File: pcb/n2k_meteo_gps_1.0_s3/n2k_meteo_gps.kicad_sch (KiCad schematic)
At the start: 33 parts, among them J10 3.3-5V, U1 LM7805_TO220, U2 ESP32-S3_SUPERMINI, U3 MCP2562-E-P, U4 PC817, U6 PC817

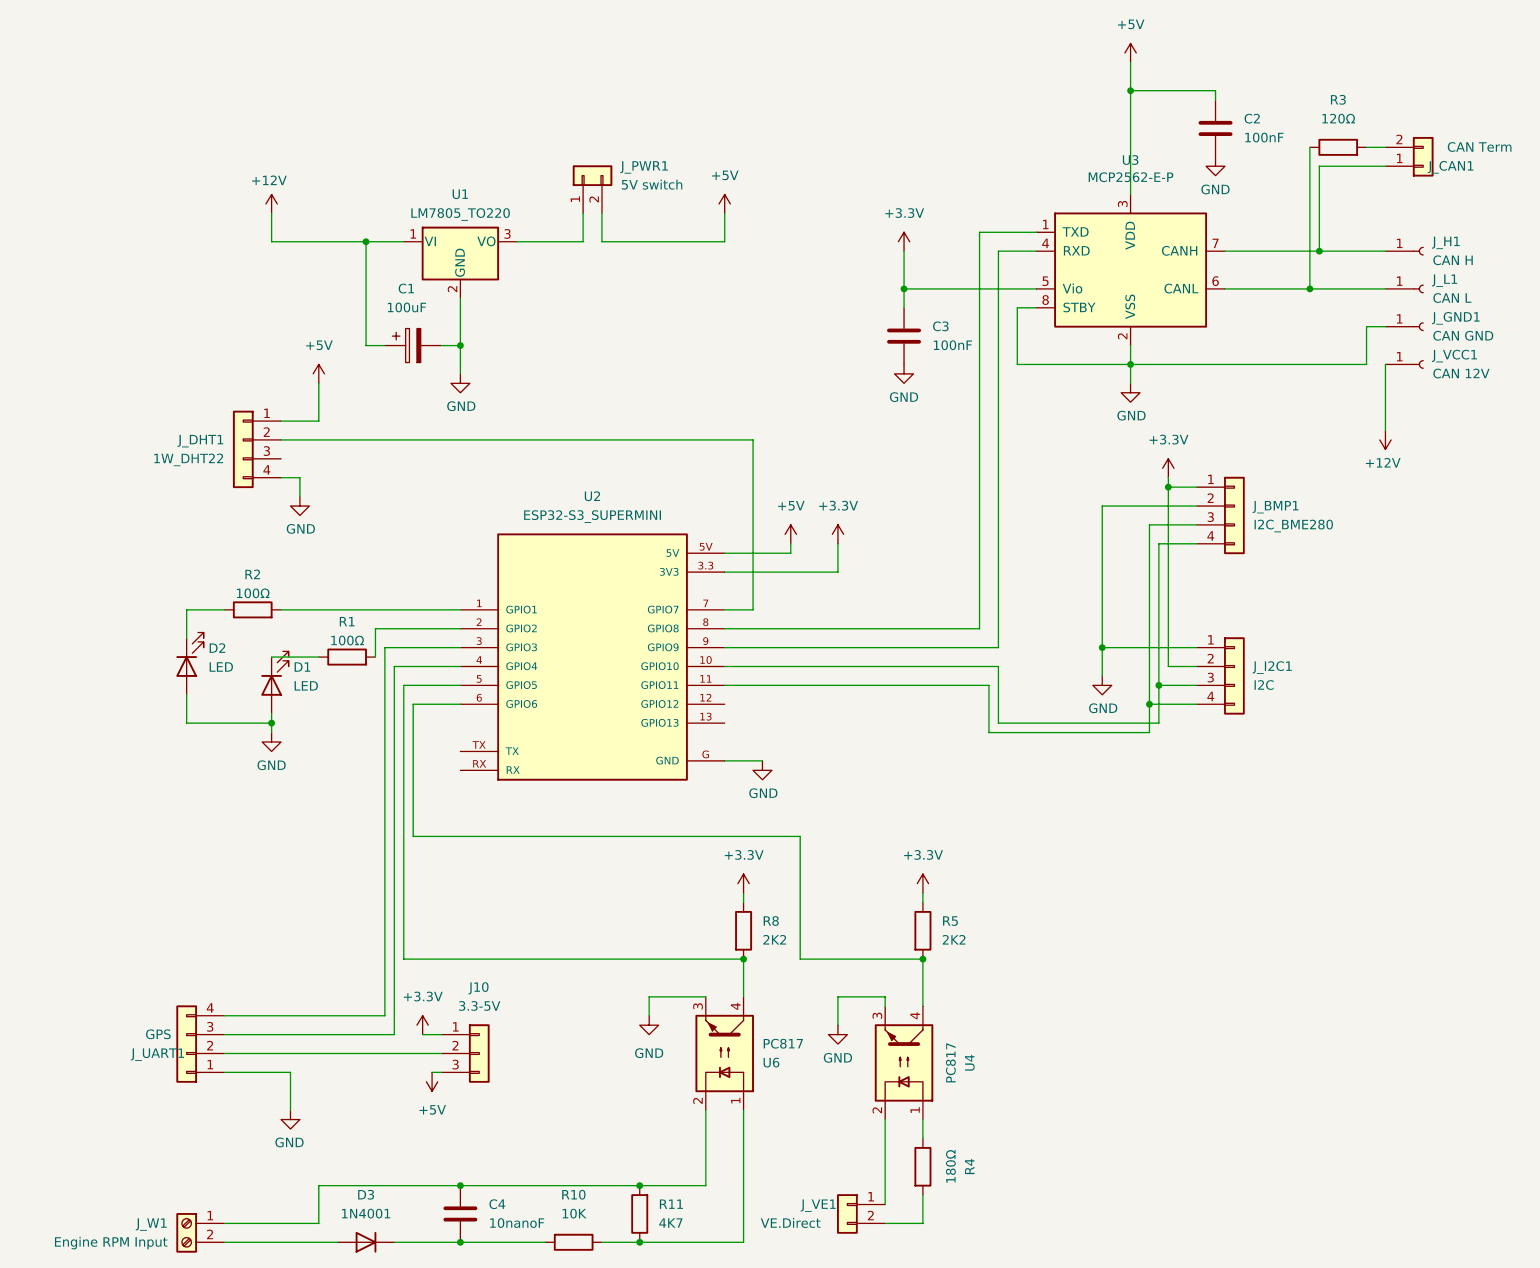
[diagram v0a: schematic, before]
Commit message: PCB - added xiao seeed studio
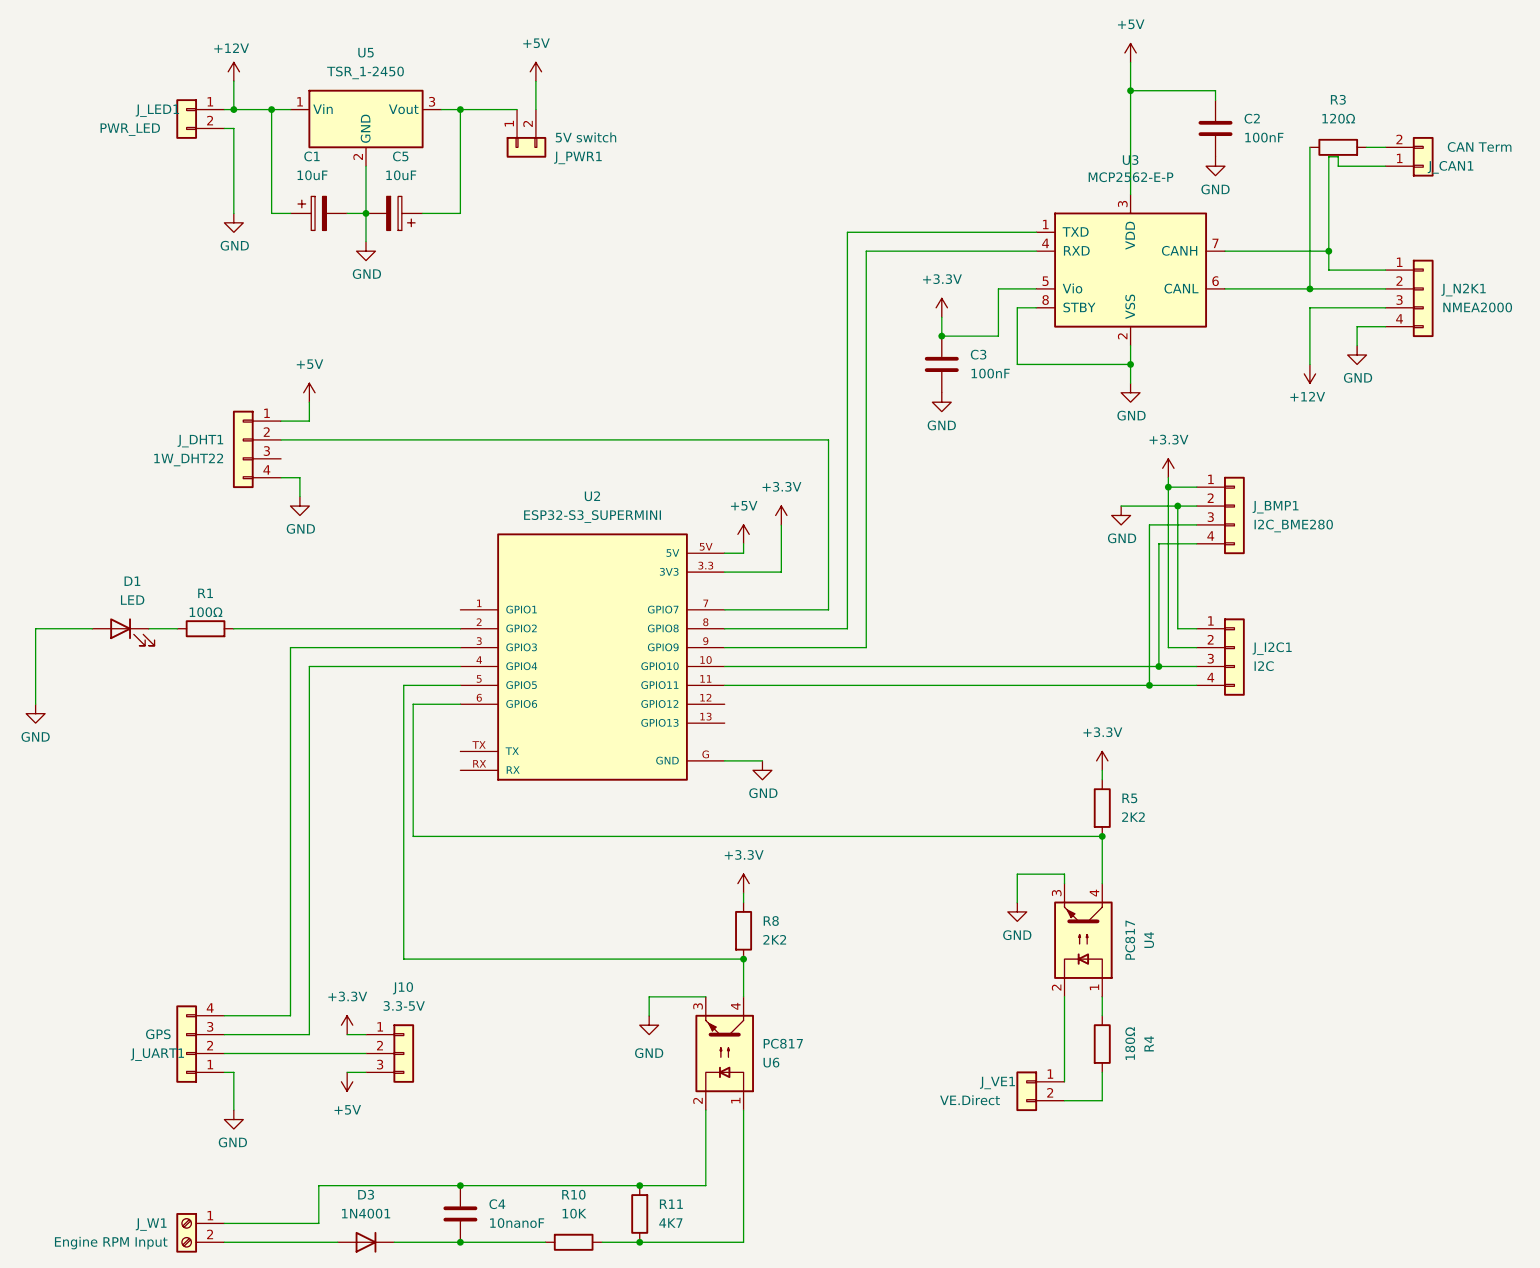
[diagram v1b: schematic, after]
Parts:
- removed D2: LED, LED_THT:LED_D3.0mm, symbol Device:LED
- removed J_GND1: CAN GND, MountingHole:MountingHole_2.2mm_M2_DIN965_Pad_TopBottom, symbol Connector:Conn_01x01_Socket
- removed J_H1: CAN H, MountingHole:MountingHole_2.2mm_M2_DIN965_Pad_TopBottom, symbol Connector:Conn_01x01_Socket
- removed J_L1: CAN L, MountingHole:MountingHole_2.2mm_M2_DIN965_Pad_TopBottom, symbol Connector:Conn_01x01_Socket
- removed J_VCC1: CAN 12V, MountingHole:MountingHole_2.2mm_M2_DIN965_Pad_TopBottom, symbol Connector:Conn_01x01_Socket
- removed R2: 100Ω, Resistor_THT:R_Axial_DIN0207_L6.3mm_D2.5mm_P7.62mm_Horizontal, symbol Device:R
- removed U1: LM7805_TO220, Package_TO_SOT_THT:TO-220-3_Vertical, symbol Regulator_Linear:LM7805_TO220
- added C5: 10uF, Capacitor_THT:C_Disc_D4.3mm_W1.9mm_P5.00mm, symbol Device:C_Polarized
- added J_LED1: PWR_LED, Connector_JST:JST_PH_B2B-PH-K_1x02_P2.00mm_Vertical, symbol Connector_Generic:Conn_01x02
- added J_N2K1: NMEA2000, Connector_JST:JST_PH_B4B-PH-K_1x04_P2.00mm_Vertical, symbol Connector_Generic:Conn_01x04
- added U5: TSR_1-2450, Converter_DCDC:Converter_DCDC_TRACO_TSR-1_THT, symbol Regulator_Switching:TSR_1-2450
- C1: value 100uF -> 10uF; footprint Capacitor_THT:CP_Radial_D10.0mm_P5.00mm -> Capacitor_THT:C_Disc_D4.3mm_W1.9mm_P5.00mm
- J_W1: footprint TerminalBlock_Phoenix:TerminalBlock_Phoenix_MKDS-1,5-2_1x02_P5.00mm_Horizontal -> TerminalBlock:TerminalBlock_bornier-2_P5.08mm
- U2: footprint Library:WAVESHARE_DEVKIT_ESP32-S3-ZERO -> MyLib:WAVESHARE_DEVKIT_ESP32-S3-ZERO
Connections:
- net +12V: now also J_LED1.1 (Pin_1), J_N2K1.3 (Pin_3), U5.1 (Vin)
- net GND: now also C5.2, J_LED1.2 (Pin_2), J_N2K1.4 (Pin_4), U5.2 (GND)
- net at R3.1, U3.6 (CANL): now also J_N2K1.2 (Pin_2)
- net at J_CAN1.1 (Pin_1), U3.7 (CANH): now also J_N2K1.1 (Pin_1)
- net at J_PWR1.1 (Pin_1): now also C5.1, U5.3 (Vout)
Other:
- moved on the sheet: C1, C3, D1, J10, J_I2C1, J_PWR1, J_VE1, R1, R4, R5, U4

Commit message: PCB
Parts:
- removed C5: 10uF, Capacitor_THT:C_Disc_D4.3mm_W1.9mm_P5.00mm, symbol Device:C_Polarized
- removed J_LED1: PWR_LED, Connector_JST:JST_PH_B2B-PH-K_1x02_P2.00mm_Vertical, symbol Connector_Generic:Conn_01x02
- removed J_N2K1: NMEA2000, Connector_JST:JST_PH_B4B-PH-K_1x04_P2.00mm_Vertical, symbol Connector_Generic:Conn_01x04
- removed U5: TSR_1-2450, Converter_DCDC:Converter_DCDC_TRACO_TSR-1_THT, symbol Regulator_Switching:TSR_1-2450
- added D2: LED, LED_THT:LED_D3.0mm, symbol Device:LED
- added J_GND1: CAN GND, MountingHole:MountingHole_2.2mm_M2_DIN965_Pad_TopBottom, symbol Connector:Conn_01x01_Socket
- added J_H1: CAN H, MountingHole:MountingHole_2.2mm_M2_DIN965_Pad_TopBottom, symbol Connector:Conn_01x01_Socket
- added J_L1: CAN L, MountingHole:MountingHole_2.2mm_M2_DIN965_Pad_TopBottom, symbol Connector:Conn_01x01_Socket
- added J_VCC1: CAN 12V, MountingHole:MountingHole_2.2mm_M2_DIN965_Pad_TopBottom, symbol Connector:Conn_01x01_Socket
- added R2: 100Ω, Resistor_THT:R_Axial_DIN0207_L6.3mm_D2.5mm_P7.62mm_Horizontal, symbol Device:R
- added U1: LM7805_TO220, Package_TO_SOT_THT:TO-220-3_Vertical, symbol Regulator_Linear:LM7805_TO220
- C1: value 10uF -> 100uF; footprint Capacitor_THT:C_Disc_D4.3mm_W1.9mm_P5.00mm -> Capacitor_THT:CP_Radial_D10.0mm_P5.00mm
- J_W1: footprint TerminalBlock:TerminalBlock_bornier-2_P5.08mm -> TerminalBlock_Phoenix:TerminalBlock_Phoenix_MKDS-1,5-2_1x02_P5.00mm_Horizontal
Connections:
- net +12V: now also J_VCC1.1 (Pin_1), U1.1 (VI)
- net GND: now also D2.2 (A), J_GND1.1 (Pin_1), U1.2 (GND)
- net at R3.1, U3.6 (CANL): now also J_L1.1 (Pin_1)
- net at J_CAN1.1 (Pin_1), U3.7 (CANH): now also J_H1.1 (Pin_1)
- net at U2.1 (GPIO1): now also R2.2
- net at J_PWR1.1 (Pin_1): now also U1.3 (VO)
- new net: D2.1 (K), R2.1
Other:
- moved on the sheet: C1, C3, D1, J10, J_I2C1, J_PWR1, J_VE1, R1, R4, R5, U4
